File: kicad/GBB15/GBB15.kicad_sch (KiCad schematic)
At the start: 72 parts, among them J1 CAN_IN, J10 USB_C_Receptacle_USB2.0, J2 CAN_OUT, J3 M0_THERM, J4 M1_THERM, J5 Conn_01x04_Male, J6 Conn_01x04_Male, J7 ENDSTOP1, J8 ENDSTOP2, SW1 SW_Push, SW2 SW_Push, U1 TMC2209-LA-T, U2 STM32G0B1CEU6, U3 TMC2209-LA-T, U4 MAX3051EKA+T, U5 NCP730BMT330TBG, Y1 Crystal_GND24

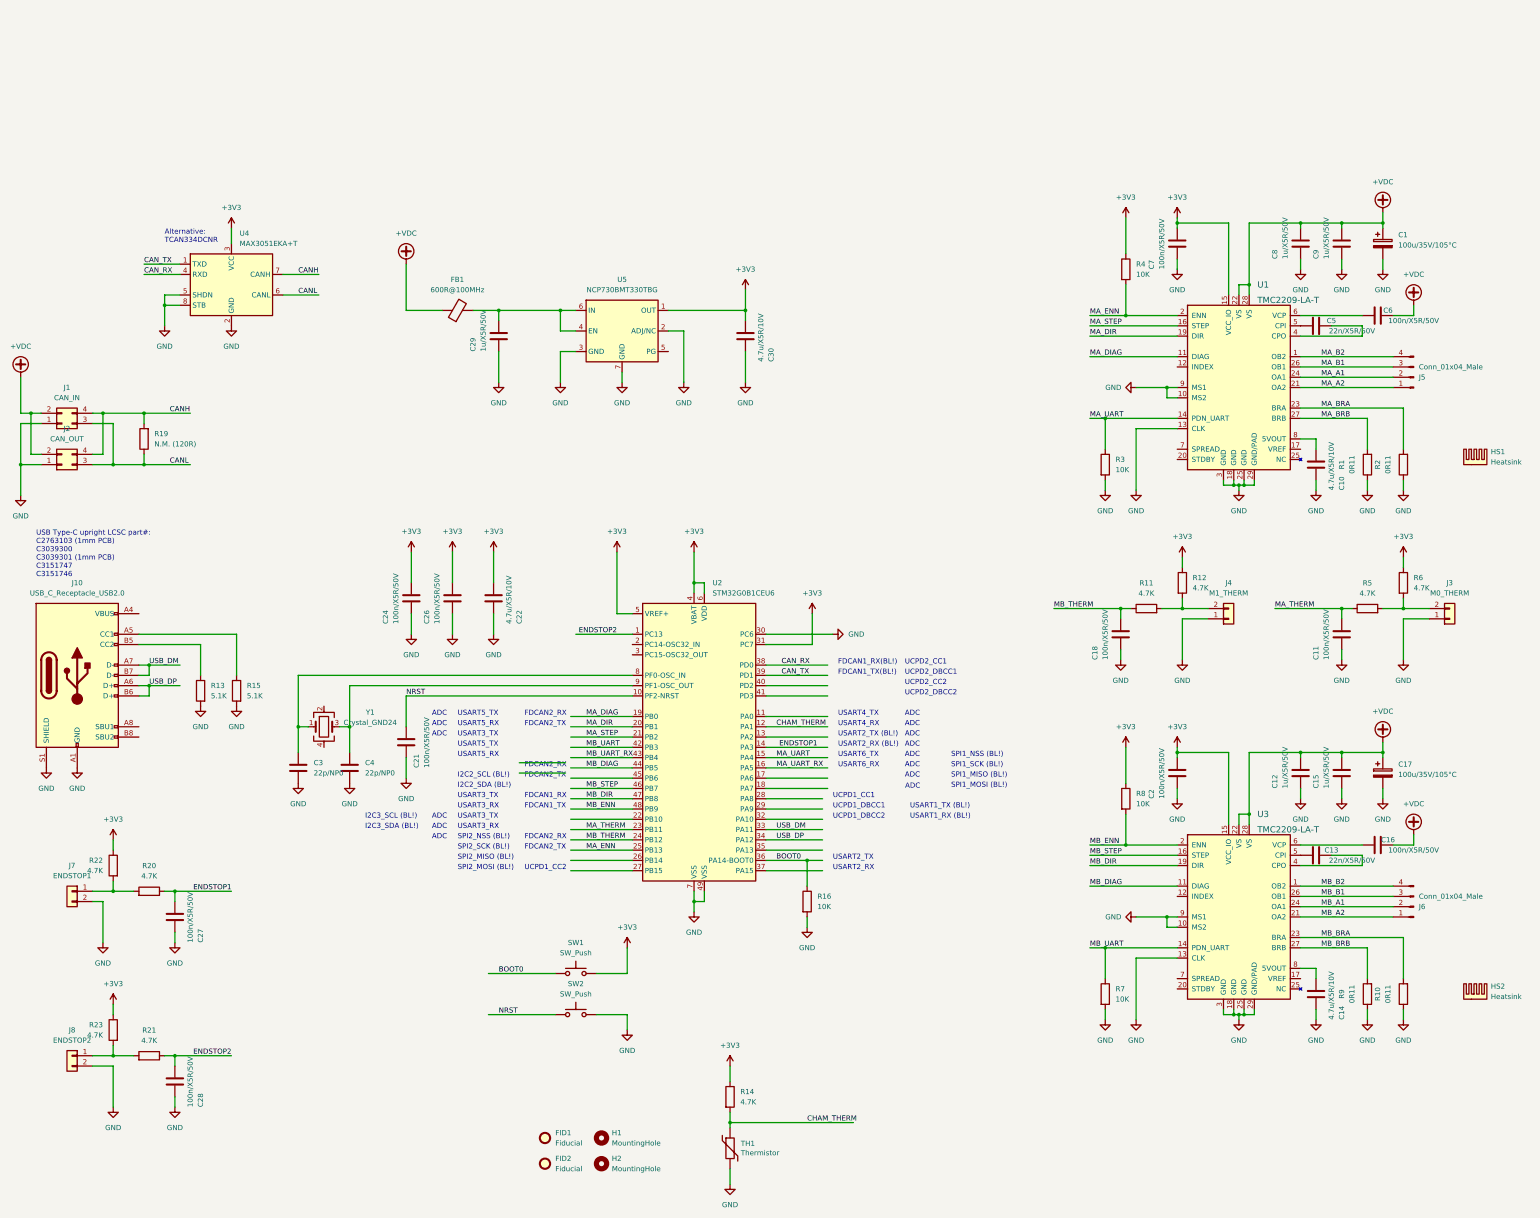
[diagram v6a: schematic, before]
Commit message: Bumped revision to B, added Power LED and moved ENDSTOP2 to ADC pin
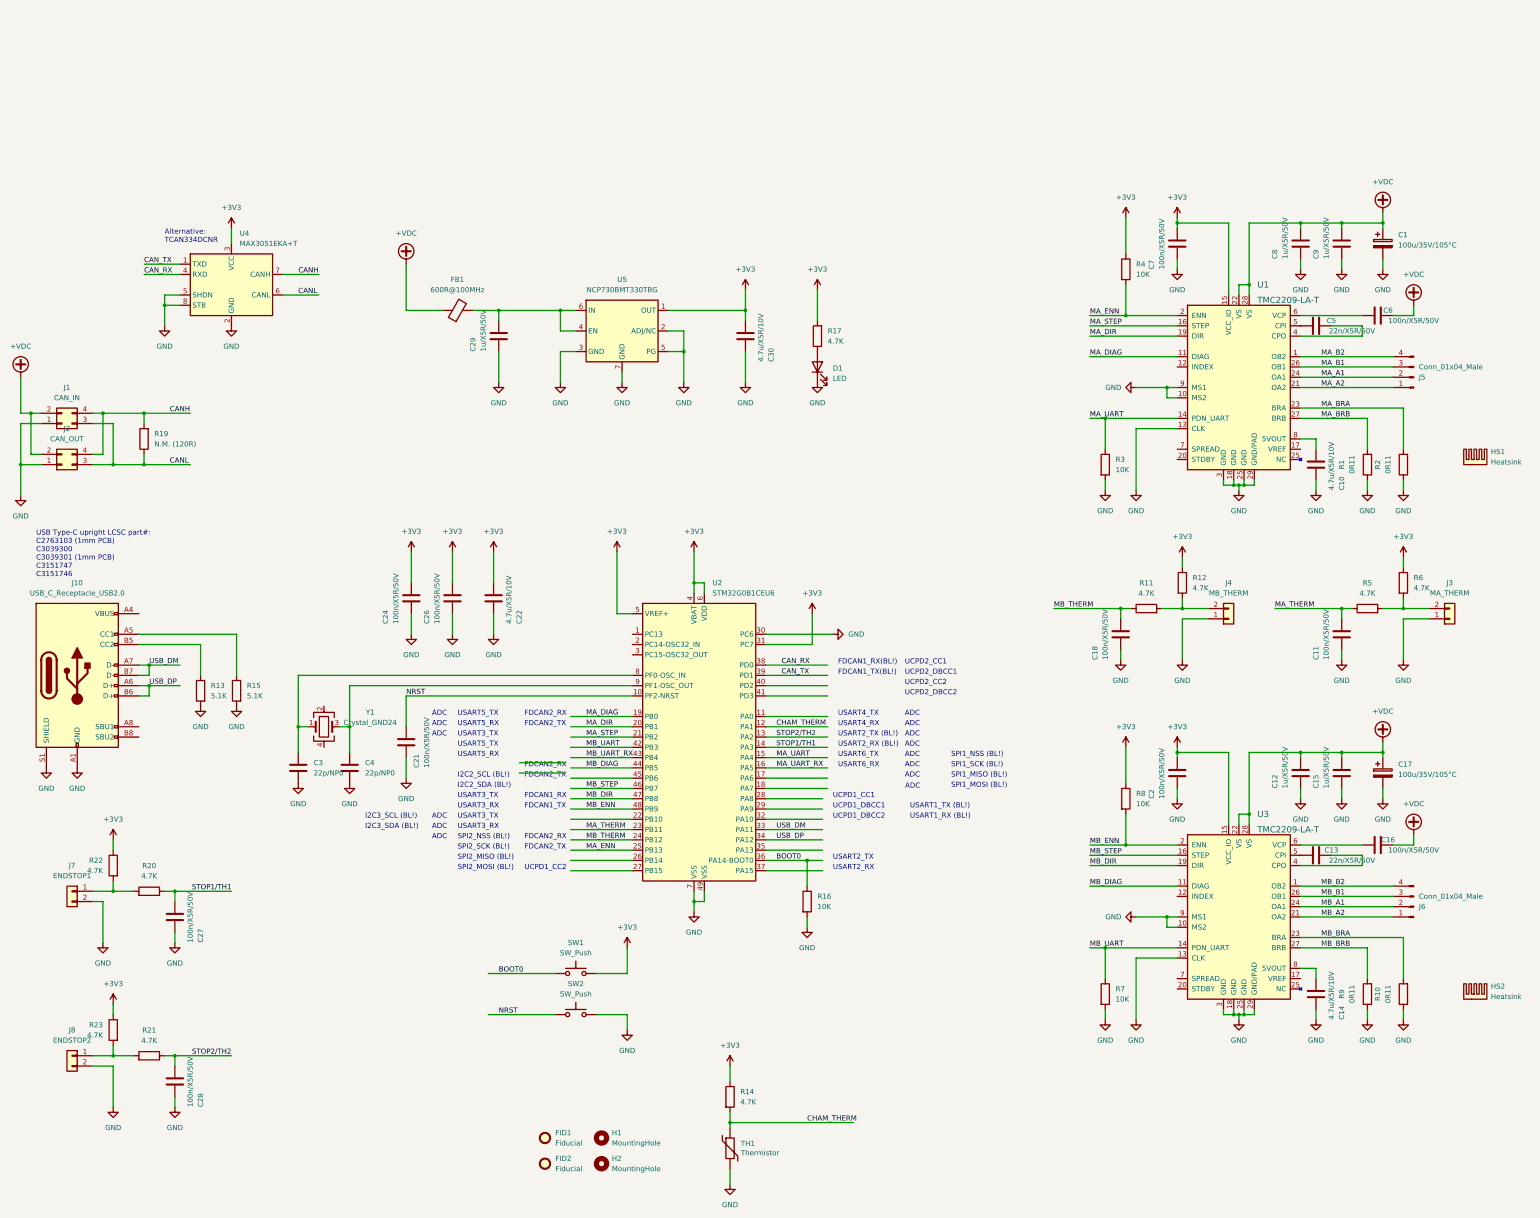
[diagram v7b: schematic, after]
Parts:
- added D1: LED, LED_SMD:LED_0603_1608Metric, symbol Device:LED
- added R17: 4.7K, Resistor_SMD:R_0603_1608Metric, symbol Device:R
- J3: value M0_THERM -> MA_THERM
- J4: value M1_THERM -> MB_THERM
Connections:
- net +3V3: now also R17.2
- net GND: now also U5.5 (PG), D1.1 (K)
- net STOP2/TH2: now reaches U2.13 (PA2)
- net STOP2/TH2: now also C28.2, R21.1
- net ENDSTOP1 renamed STOP1/TH1
- removed net ENDSTOP2: C28.2, R21.1, U2.1 (PC13)
- new net: D1.2 (A), R17.1
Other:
- title: (none) -> Gantry-Board GBB15
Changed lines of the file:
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@@
 (kicad_sch (version 20211123) (generator eeschema)
   (paper "A3")
+  (title_block
+    (title "Gantry-Board GBB15")
+    (rev "B")
+  )
   (junction (at 311.15 195.58) (diameter 0) (color 0 0 0 0)
   )
@@
   (junction (at 364.49 24.13) (diameter 0) (color 0 0 0 0)
   )
+  (junction (at 191.77 55.88) (diameter 0) (color 0 0 0 0)
+  )
   (junction (at 311.15 64.77) (diameter 0) (color 0 0 0 0)
   )
@@
     (stroke (width 0) (type default) (color 0 0 0 0))
   )
+  (wire (pts (xy 224.79 40.64) (xy 224.79 48.26))
+    (stroke (width 0) (type default) (color 0 0 0 0))
+  )
   (wire (pts (xy 300.99 22.86) (xy 300.99 31.75))
     (stroke (width 0) (type default) (color 0 0 0 0))
@@
     (stroke (width 0) (type default) (color 0 0 0 0))
   )
-  (wire (pts (xy 165.1 125.73) (xy 179.07 125.73))
-    (stroke (width 0) (type default) (color 0 0 0 0))
-  )
   (wire (pts (xy 144.78 120.65) (xy 144.78 125.73))
     (stroke (width 0) (type default) (color 0 0 0 0))
@@
     (stroke (width 0) (type default) (color 0 0 0 0))
   )
-  (wire (pts (xy 191.77 50.8) (xy 191.77 63.5))
+  (wire (pts (xy 191.77 50.8) (xy 191.77 55.88))
     (stroke (width 0) (type default) (color 0 0 0 0))
   )
@@
     (stroke (width 0) (type default) (color 0 0 0 0))
   )
+  (wire (pts (xy 187.96 55.88) (xy 191.77 55.88))
+    (stroke (width 0) (type default) (color 0 0 0 0))
+  )
   (wire (pts (xy 48.26 81.28) (xy 48.26 71.12))
     (stroke (width 0) (type default) (color 0 0 0 0))
@@
     (stroke (width 0) (type default) (color 0 0 0 0))
   )
+  (wire (pts (xy 191.77 55.88) (xy 191.77 63.5))
+    (stroke (width 0) (type default) (color 0 0 0 0))
+  )
   (wire (pts (xy 212.09 135.89) (xy 227.33 135.89))
     (stroke (width 0) (type default) (color 0 0 0 0))
@@
     (effects (font (size 1.27 1.27)) (justify left bottom))
   )
-  (label "ENDSTOP1" (at 224.79 153.67 180)
-    (effects (font (size 1.27 1.27)) (justify right bottom))
+  (label "STOP1{slash}TH1" (at 214.63 153.67 0)
+    (effects (font (size 1.27 1.27)) (justify left bottom))
   )
   (label "CANL" (at 96.52 41.91 0)
@@
     (effects (font (size 1.27 1.27)) (justify left bottom))
   )
-  (label "ENDSTOP1" (at 80.01 189.23 180)
+  (label "STOP1{slash}TH1" (at 80.01 189.23 180)
     (effects (font (size 1.27 1.27)) (justify right bottom))
   )
@@
     (effects (font (size 1.27 1.27)) (justify left bottom))
   )
-  (label "ENDSTOP2" (at 80.01 229.87 180)
+  (label "STOP2{slash}TH2" (at 80.01 229.87 180)
     (effects (font (size 1.27 1.27)) (justify right bottom))
   )
@@
     (effects (font (size 1.27 1.27)) (justify left bottom))
   )
-  (label "ENDSTOP2" (at 175.26 125.73 180)
-    (effects (font (size 1.27 1.27)) (justify right bottom))
+  (label "STOP2{slash}TH2" (at 214.63 151.13 0)
+    (effects (font (size 1.27 1.27)) (justify left bottom))
   )
   (label "MA_B2" (at 349.25 57.15 0)
@@
     (in_bom yes) (on_board yes) (fields_autoplaced)
     (property "Reference" "J4" (id 0) (at 326.39 113.03 0))
-    (property "Value" "M1_THERM" (id 1) (at 326.39 115.57 0))
+    (property "Value" "MB_THERM" (id 1) (at 326.39 115.57 0))
     (property "Footprint" "Connector_JST:JST_PH_B2B-PH-K_1x02_P2.00mm_Vertical" (id 2) (at 326.39 121.92 0)
       (effects (font (size 1.27 1.27)) hide)
@@
     (in_bom yes) (on_board yes) (fields_autoplaced)
     (property "Reference" "J3" (id 0) (at 381 113.03 0))
-    (property "Value" "M0_THERM" (id 1) (at 381 115.57 0))
+    (property "Value" "MA_THERM" (id 1) (at 381 115.57 0))
     (property "Footprint" "Connector_JST:JST_PH_B2B-PH-K_1x02_P2.00mm_Vertical" (id 2) (at 381 121.92 0)
       (effects (font (size 1.27 1.27)) hide)
@@
     )
   )
+  (symbol (lib_id "power:GND") (at 224.79 63.5 0) (unit 1)
+    (in_bom yes) (on_board yes) (fields_autoplaced)
+    (property "Reference" "#PWR02" (id 0) (at 224.79 69.85 0)
+      (effects (font (size 1.27 1.27)) hide)
+    )
+    (property "Value" "GND" (id 1) (at 224.79 68.58 0))
+    (property "Footprint" "" (id 2) (at 224.79 63.5 0)
+      (effects (font (size 1.27 1.27)) hide)
+    )
+    (property "Datasheet" "" (id 3) (at 224.79 63.5 0)
+      (effects (font (size 1.27 1.27)) hide)
+    )
+    (pin "1")
+  )
   (symbol (lib_id "power:GND") (at 364.49 35.56 0) (unit 1)
     (in_bom yes) (on_board yes) (fields_autoplaced)
@@
     (pin "1")
   )
+  (symbol (lib_id "power:+3V3") (at 224.79 40.64 0) (unit 1)
+    (in_bom yes) (on_board yes) (fields_autoplaced)
+    (property "Reference" "#PWR01" (id 0) (at 224.79 44.45 0)
+      (effects (font (size 1.27 1.27)) hide)
+    )
+    (property "Value" "+3V3" (id 1) (at 224.79 35.56 0))
+    (property "Footprint" "" (id 2) (at 224.79 40.64 0)
+      (effects (font (size 1.27 1.27)) hide)
+    )
+    (property "Datasheet" "" (id 3) (at 224.79 40.64 0)
+      (effects (font (size 1.27 1.27)) hide)
+    )
+    (pin "1")
+  )
+  (symbol (lib_id "Device:LED") (at 224.79 59.69 90) (unit 1)
+    (in_bom yes) (on_board yes) (fields_autoplaced)
+    (property "Reference" "D1" (id 0) (at 228.6 60.0074 90)
+      (effects (font (size 1.27 1.27)) (justify right))
+    )
+    (property "Value" "LED" (id 1) (at 228.6 62.5474 90)
+      (effects (font (size 1.27 1.27)) (justify right))
+    )
+    (property "Footprint" "LED_SMD:LED_0603_1608Metric" (id 2) (at 224.79 59.69 0)
+      (effects (font (size 1.27 1.27)) hide)
+    )
+    (property "Datasheet" "~" (id 3) (at 224.79 59.69 0)
+      (effects (font (size 1.27 1.27)) hide)
+    )
+    (property "LCSC" "C72043" (id 4) (at 224.79 59.69 90)
+      (effects (font (size 1.27 1.27)) hide)
+    )
+    (pin "1")
+    (pin "2")
+  )
   (symbol (lib_id "power:GND") (at 144.78 125.73 0) (unit 1)
     (in_bom yes) (on_board yes) (fields_autoplaced)
@@
     (pin "1")
   )
+  (symbol (lib_id "Device:R") (at 224.79 52.07 180) (unit 1)
+    (in_bom yes) (on_board yes) (fields_autoplaced)
+    (property "Reference" "R17" (id 0) (at 227.33 50.7999 0)
+      (effects (font (size 1.27 1.27)) (justify right))
+    )
+    (property "Value" "4.7K" (id 1) (at 227.33 53.3399 0)
+      (effects (font (size 1.27 1.27)) (justify right))
+    )
+    (property "Footprint" "Resistor_SMD:R_0603_1608Metric" (id 2) (at 226.568 52.07 90)
+      (effects (font (size 1.27 1.27)) hide)
+    )
+    (property "Datasheet" "~" (id 3) (at 224.79 52.07 0)
+      (effects (font (size 1.27 1.27)) hide)
+    )
+    (property "LCSC" "C23162" (id 4) (at 218.4902 52.07 0)
+      (effects (font (size 1.27 1.27)) hide)
+    )
+    (pin "1")
+    (pin "2")
+  )
   (symbol (lib_id "power:+VDC") (at 27.94 62.23 0) (unit 1)
     (in_bom yes) (on_board yes) (fields_autoplaced)
@@
   )
   (symbol_instances
+    (path "/999ec898-e392-471d-8c58-983d6dbf5998"
+      (reference "#PWR01") (unit 1) (value "+3V3") (footprint "")
+    )
+    (path "/8f183059-1f9c-4c3b-8463-c485df16f55b"
+      (reference "#PWR02") (unit 1) (value "GND") (footprint "")
+    )
     (path "/f2e31222-6361-4435-b7bd-e6ca8eb97127"
       (reference "#PWR0101") (unit 1) (value "GND") (footprint "")
@@
       (reference "C30") (unit 1) (value "4.7u/X5R/10V") (footprint "Capacitor_SMD:C_0603_1608Metric")
     )
+    (path "/9c06e32c-8c7c-4c00-af04-05280a8b49ad"
+      (reference "D1") (unit 1) (value "LED") (footprint "LED_SMD:LED_0603_1608Metric")
+    )
     (path "/ba18025c-7546-4e55-a8a0-4bcd4f6f4d31"
       (reference "FB1") (unit 1) (value "600R@100MHz") (footprint "Inductor_SMD:L_0603_1608Metric")
@@
     )
     (path "/19dfe9a3-bbb7-4883-865d-fe856a27b537"
-      (reference "J3") (unit 1) (value "M0_THERM") (footprint "Connector_JST:JST_PH_B2B-PH-K_1x02_P2.00mm_Vertical")
+      (reference "J3") (unit 1) (value "MA_THERM") (footprint "Connector_JST:JST_PH_B2B-PH-K_1x02_P2.00mm_Vertical")
     )
     (path "/004ddc44-7042-4b60-8ce0-84158061ee16"
-      (reference "J4") (unit 1) (value "M1_THERM") (footprint "Connector_JST:JST_PH_B2B-PH-K_1x02_P2.00mm_Vertical")
+      (reference "J4") (unit 1) (value "MB_THERM") (footprint "Connector_JST:JST_PH_B2B-PH-K_1x02_P2.00mm_Vertical")
     )
     (path "/9d8076e4-90bf-434d-b742-fd981c971465"
@@
       (reference "R16") (unit 1) (value "10K") (footprint "Resistor_SMD:R_0603_1608Metric")
     )
+    (path "/ad54a3a9-8f3b-4f3d-89a1-c50ee44c679c"
+      (reference "R17") (unit 1) (value "4.7K") (footprint "Resistor_SMD:R_0603_1608Metric")
+    )
     (path "/dcd12b4a-ad4d-4b1a-b0d4-dafc0b86253e"
